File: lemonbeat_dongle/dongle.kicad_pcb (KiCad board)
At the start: 4 copper layers, 50 x 20 mm, 75 parts, among them J201 USB_A, J202 Prog, J203 u.FL, J301 SMA, SW201 SW_Push, U201 nRF52840, U301 Si4467, Y201 32MHz, Y202 32.768kHz, Y301 26MHz

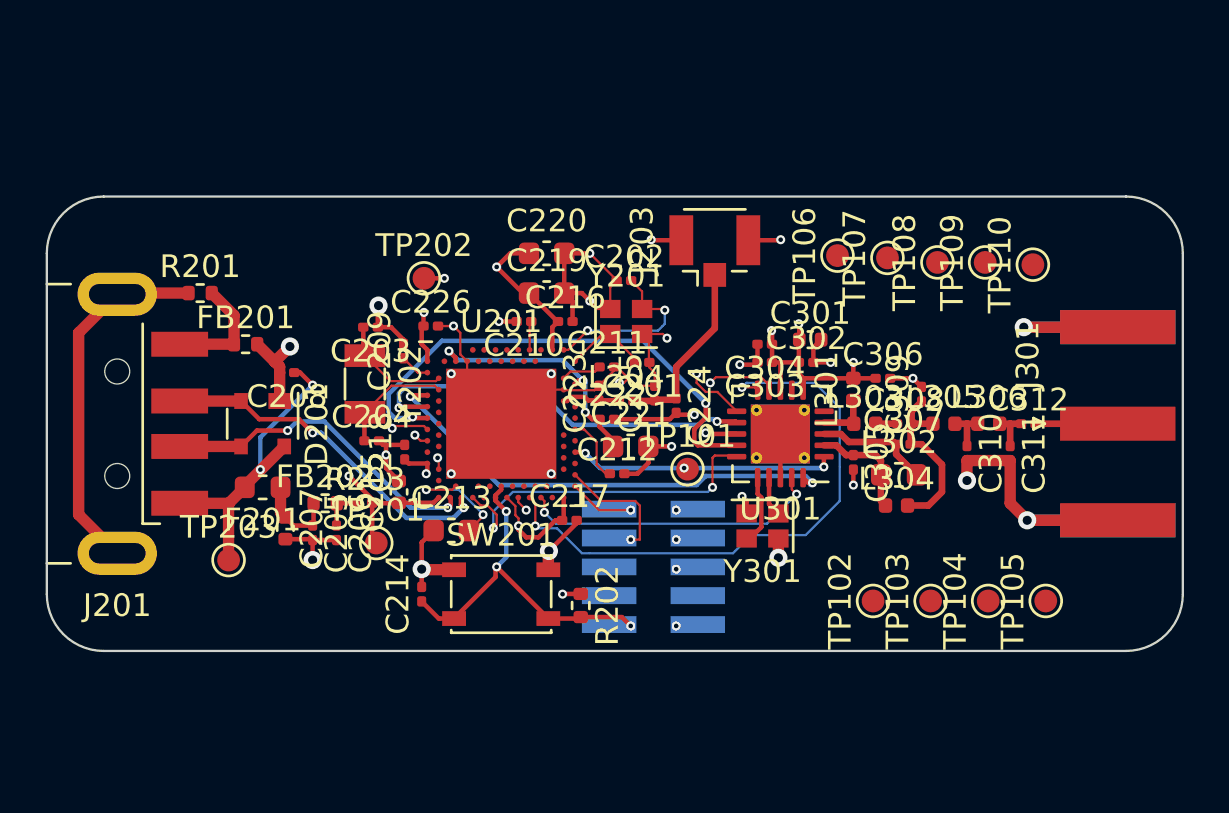
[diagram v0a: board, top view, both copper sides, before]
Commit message: dongle: PCB: add holes in corners
This is in preparation for mounting in a case (e.g. 3D printed).
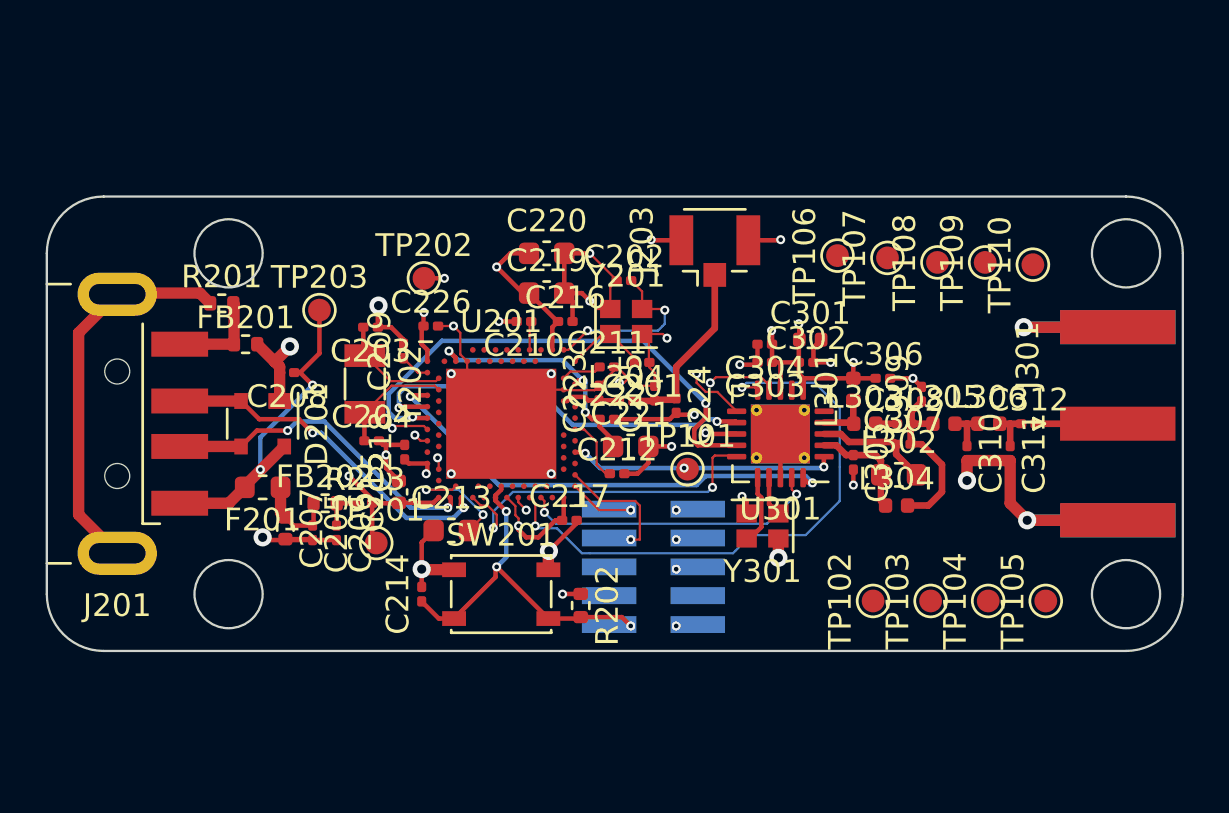
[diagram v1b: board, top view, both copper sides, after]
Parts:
- moved TP203 11.7 mm to (122.5, 99.0)
- moved R201 1.05 mm to (118.2, 98.7)
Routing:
- net GND: track 89.2 -> 90.6 mm
- net Net-(J201-Pad5): track 16.0 -> 17.1 mm
- net Net-(FB201-Pad1): track 5.05 -> 4.20 mm
- net Net-(C208-Pad1): track 13.9 -> 14.5 mm
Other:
- outline, holes or cut-outs redrawn

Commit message: dongle: PCB: add RF guard ring
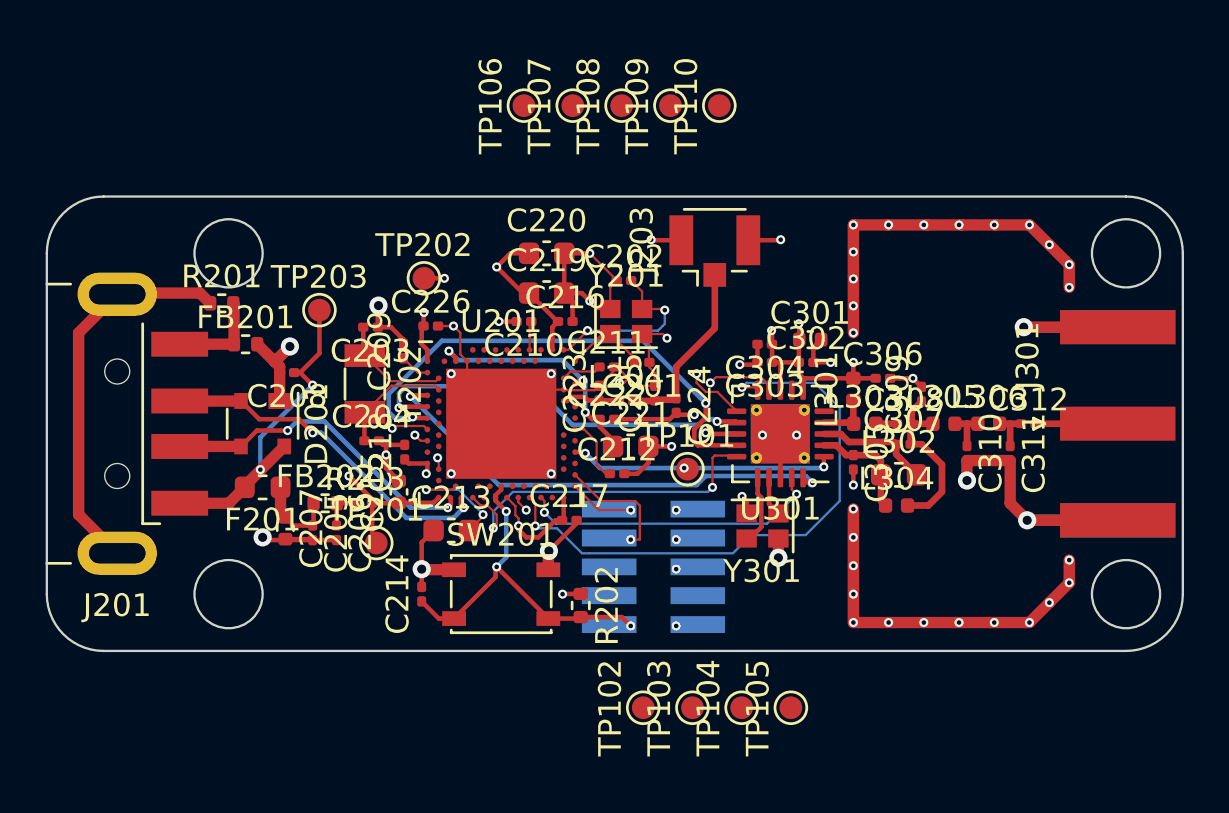
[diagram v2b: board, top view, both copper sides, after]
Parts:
- moved TP108 15.5 mm to (135.8, 90.0)
- moved TP110 15.5 mm to (140.1, 90.0)
- moved TP109 15.5 mm to (137.9, 90.0)
- moved TP107 15.4 mm to (133.7, 90.0)
- moved TP106 15.3 mm to (131.5, 90.0)
- moved TP105 12.2 mm to (143.2, 116.5)
- moved TP104 11.8 mm to (141.1, 116.5)
- moved TP103 11.5 mm to (138.9, 116.5)
- moved TP102 11.2 mm to (136.8, 116.5)
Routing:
- net (no net): track 0.00 -> 32.2 mm, vias 0 -> 26
- net GND: vias 32 -> 34
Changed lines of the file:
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@@
   )
   (footprint "TestPoint:TestPoint_Pad_D1.0mm" (layer "F.Cu")
-    (at 153.9 97 90)
+    (at 140.1 90 90)
     (descr "SMD pad as test Point, diameter 1.0mm")
     (tags "test point SMD pad")
@@
   )
   (footprint "TestPoint:TestPoint_Pad_D1.0mm" (layer "F.Cu")
-    (at 146.866667 111.8 90)
+    (at 136.75 116.5 90)
     (descr "SMD pad as test Point, diameter 1.0mm")
     (tags "test point SMD pad")
@@
   )
   (footprint "TestPoint:TestPoint_Pad_D1.0mm" (layer "F.Cu")
-    (at 154.466667 111.8 90)
+    (at 143.25 116.5 90)
     (descr "SMD pad as test Point, diameter 1.0mm")
     (tags "test point SMD pad")
@@
   )
   (footprint "TestPoint:TestPoint_Pad_D1.0mm" (layer "F.Cu")
-    (at 151.8 96.9 90)
+    (at 137.95 90 90)
     (descr "SMD pad as test Point, diameter 1.0mm")
     (tags "test point SMD pad")
@@
   )
   (footprint "TestPoint:TestPoint_Pad_D1.0mm" (layer "F.Cu")
-    (at 147.5 96.7 90)
+    (at 133.65 90 90)
     (descr "SMD pad as test Point, diameter 1.0mm")
     (tags "test point SMD pad")
@@
   )
   (footprint "TestPoint:TestPoint_Pad_D1.0mm" (layer "F.Cu")
-    (at 149.7 96.9 90)
+    (at 135.8 90 90)
     (descr "SMD pad as test Point, diameter 1.0mm")
     (tags "test point SMD pad")
@@
   )
   (footprint "TestPoint:TestPoint_Pad_D1.0mm" (layer "F.Cu")
-    (at 151.933333 111.8 90)
+    (at 141.083332 116.5 90)
     (descr "SMD pad as test Point, diameter 1.0mm")
     (tags "test point SMD pad")
@@
   )
   (footprint "TestPoint:TestPoint_Pad_D1.0mm" (layer "F.Cu")
-    (at 149.4 111.8 90)
+    (at 138.916666 116.5 90)
     (descr "SMD pad as test Point, diameter 1.0mm")
     (tags "test point SMD pad")
@@
   )
   (footprint "TestPoint:TestPoint_Pad_D1.0mm" (layer "F.Cu")
-    (at 145.3 96.6 90)
+    (at 131.5 90 90)
     (descr "SMD pad as test Point, diameter 1.0mm")
     (tags "test point SMD pad")
@@
     )
   )
+  (gr_line (start 146 95.25) (end 153.75 95.25) (layer "F.Mask") (width 0.5))
+  (gr_line (start 146 107.75) (end 146 112.75) (layer "F.Mask") (width 0.5))
+  (gr_line (start 153.75 95.25) (end 155.5 97) (layer "F.Mask") (width 0.5))
+  (gr_line (start 155.5 97) (end 155.5 98) (layer "F.Mask") (width 0.5))
+  (gr_line (start 146 112.75) (end 153.75 112.75) (layer "F.Mask") (width 0.5))
+  (gr_line (start 153.75 112.75) (end 155.5 111) (layer "F.Mask") (width 0.5))
+  (gr_line (start 155.5 111) (end 155.5 110) (layer "F.Mask") (width 0.5))
+  (gr_line (start 146 100) (end 146 95.25) (layer "F.Mask") (width 0.5))
   (gr_circle (center 158 96.5) (end 159.5 96.5) (layer "Edge.Cuts") (width 0.1) (fill none))
   (gr_arc (start 158 94) (mid 159.767767 94.732233) (end 160.5 96.5) (layer "Edge.Cuts") (width 0.1))
@@
   (gr_arc (start 160.5 111.5) (mid 159.767767 113.267767) (end 158 114) (layer "Edge.Cuts") (width 0.1))
   (gr_line (start 113 94) (end 158 94) (layer "Edge.Cuts") (width 0.1))
+  (segment (start 152.25 95.25) (end 153.75 95.25) (width 0.5) (layer "F.Cu") (net 0))
+  (segment (start 147.5 95.25) (end 149.25 95.25) (width 0.5) (layer "F.Cu") (net 0))
+  (segment (start 154.625 96.125) (end 155.5 97) (width 0.5) (layer "F.Cu") (net 0))
+  (segment (start 146 97.5) (end 146 96.25) (width 0.5) (layer "F.Cu") (net 0))
+  (segment (start 154.625 111.875) (end 153.75 112.75) (width 0.5) (layer "F.Cu") (net 0))
+  (segment (start 147.5 112.75) (end 146 112.75) (width 0.5) (layer "F.Cu") (net 0))
+  (segment (start 146 110.25) (end 146 109) (width 0.5) (layer "F.Cu") (net 0))
+  (segment (start 146 100) (end 146 98.75) (width 0.5) (layer "F.Cu") (net 0))
+  (segment (start 146 98.75) (end 146 97.5) (width 0.5) (layer "F.Cu") (net 0))
+  (segment (start 149.25 95.25) (end 150.75 95.25) (width 0.5) (layer "F.Cu") (net 0))
+  (segment (start 152 112.75) (end 150.5 112.75) (width 0.5) (layer "F.Cu") (net 0))
+  (segment (start 146 112.75) (end 146 111.25) (width 0.5) (layer "F.Cu") (net 0))
+  (segment (start 150.5 112.75) (end 149 112.75) (width 0.5) (layer "F.Cu") (net 0))
+  (segment (start 153.75 112.75) (end 152 112.75) (width 0.5) (layer "F.Cu") (net 0))
+  (segment (start 146 111.25) (end 146 110.25) (width 0.5) (layer "F.Cu") (net 0))
+  (segment (start 146 96.25) (end 146 95.25) (width 0.5) (layer "F.Cu") (net 0))
+  (segment (start 146 109) (end 146 107.75) (width 0.5) (layer "F.Cu") (net 0))
+  (segment (start 149 112.75) (end 147.5 112.75) (width 0.5) (layer "F.Cu") (net 0))
+  (segment (start 155.5 97) (end 155.5 98) (width 0.5) (layer "F.Cu") (net 0))
+  (segment (start 154.625 96.125) (end 153.75 95.25) (width 0.5) (layer "F.Cu") (net 0))
+  (segment (start 155.5 111) (end 155.5 110) (width 0.5) (layer "F.Cu") (net 0))
+  (segment (start 150.75 95.25) (end 152.25 95.25) (width 0.5) (layer "F.Cu") (net 0))
+  (segment (start 155.5 111) (end 154.625 111.875) (width 0.5) (layer "F.Cu") (net 0))
+  (segment (start 146 95.25) (end 147.5 95.25) (width 0.5) (layer "F.Cu") (net 0))
+  (via (at 154.625 96.125) (size 0.4) (drill 0.2) (layers "F.Cu" "B.Cu") (net 0))
+  (via (at 146 98.8125) (size 0.4) (drill 0.2) (layers "F.Cu" "B.Cu") (net 0))
+  (via (at 150.65 95.25) (size 0.4) (drill 0.2) (layers "F.Cu" "B.Cu") (net 0))
+  (via (at 152.2 95.25) (size 0.4) (drill 0.2) (layers "F.Cu" "B.Cu") (net 0))
+  (via (at 146 109) (size 0.4) (drill 0.2) (layers "F.Cu" "B.Cu") (net 0))
+  (via (at 147.55 112.75) (size 0.4) (drill 0.2) (layers "F.Cu" "B.Cu") (net 0))
+  (via (at 146 95.25) (size 0.4) (drill 0.2) (layers "F.Cu" "B.Cu") (net 0))
+  (via (at 152.2 112.75) (size 0.4) (drill 0.2) (layers "F.Cu" "B.Cu") (net 0))
+  (via (at 155.5 111) (size 0.4) (drill 0.2) (layers "F.Cu" "B.Cu") (net 0))
+  (via (at 146 111.5) (size 0.4) (drill 0.2) (layers "F.Cu" "B.Cu") (net 0))
+  (via (at 155.5 97) (size 0.4) (drill 0.2) (layers "F.Cu" "B.Cu") (net 0))
+  (via (at 155.5 110) (size 0.4) (drill 0.2) (layers "F.Cu" "B.Cu") (net 0))
+  (via (at 149.1 95.25) (size 0.4) (drill 0.2) (layers "F.Cu" "B.Cu") (net 0))
+  (via (at 150.65 112.75) (size 0.4) (drill 0.2) (layers "F.Cu" "B.Cu") (net 0))
+  (via (at 146 97.625) (size 0.4) (drill 0.2) (layers "F.Cu" "B.Cu") (net 0))
+  (via (at 146 100) (size 0.4) (drill 0.2) (layers "F.Cu" "B.Cu") (net 0))
+  (via (at 147.55 95.25) (size 0.4) (drill 0.2) (layers "F.Cu" "B.Cu") (net 0))
+  (via (at 153.75 112.75) (size 0.4) (drill 0.2) (layers "F.Cu" "B.Cu") (net 0))
+  (via (at 146 96.4375) (size 0.4) (drill 0.2) (layers "F.Cu" "B.Cu") (net 0))
+  (via (at 146 112.75) (size 0.4) (drill 0.2) (layers "F.Cu" "B.Cu") (net 0))
+  (via (at 149.1 112.75) (size 0.4) (drill 0.2) (layers "F.Cu" "B.Cu") (net 0))
+  (via (at 146 107.75) (size 0.4) (drill 0.2) (layers "F.Cu" "B.Cu") (net 0))
+  (via (at 146 110.25) (size 0.4) (drill 0.2) (layers "F.Cu" "B.Cu") (net 0))
+  (via (at 155.5 98) (size 0.4) (drill 0.2) (layers "F.Cu" "B.Cu") (net 0))
+  (via (at 153.75 95.25) (size 0.4) (drill 0.2) (layers "F.Cu" "B.Cu") (net 0))
+  (via (at 154.625 111.875) (size 0.4) (drill 0.2) (layers "F.Cu" "B.Cu") (net 0))
   (segment (start 122.16 109.08) (end 122.2 109.12) (width 0.2) (layer "F.Cu") (net 1))
   (segment (start 141.3 107.4) (end 141.1 107.2) (width 0.2) (layer "F.Cu") (net 1))
@@
   (via (at 132.7 101.8) (size 0.4) (drill 0.2) (layers "F.Cu" "B.Cu") (net 1))
   (via (at 128.3 101.8) (size 0.4) (drill 0.2) (layers "F.Cu" "B.Cu") (net 1))
+  (via (at 143.5 104.5) (size 0.4) (drill 0.2) (layers "F.Cu" "B.Cu") (net 1))
   (via (at 130.4 99.5) (size 0.4) (drill 0.2) (layers "F.Cu" "B.Cu") (net 1))
   (via (at 132.7 106.2) (size 0.4) (drill 0.2) (layers "F.Cu" "B.Cu") (net 1))
@@
   (via (at 139 103.6) (size 0.4) (drill 0.2) (layers "F.Cu" "B.Cu") (net 1))
   (via (at 153.65 108.25) (size 0.8) (drill 0.4) (layers "F.Cu" "B.Cu") (net 1))
+  (via (at 142 104.5) (size 0.4) (drill 0.2) (layers "F.Cu" "B.Cu") (net 1))
   (via (at 142.8 95.9) (size 0.4) (drill 0.2) (layers "F.Cu" "B.Cu") (net 1))
   (via (at 132.6 109.6) (size 0.8) (drill 0.4) (layers "F.Cu" "B.Cu") (net 1))

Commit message: dongle: PCB: connect RF guard ring to GND net
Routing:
- net (no net): track 32.2 -> 0.00 mm, vias 26 -> 0
- net GND: track 90.6 -> 122.8 mm, vias 34 -> 60

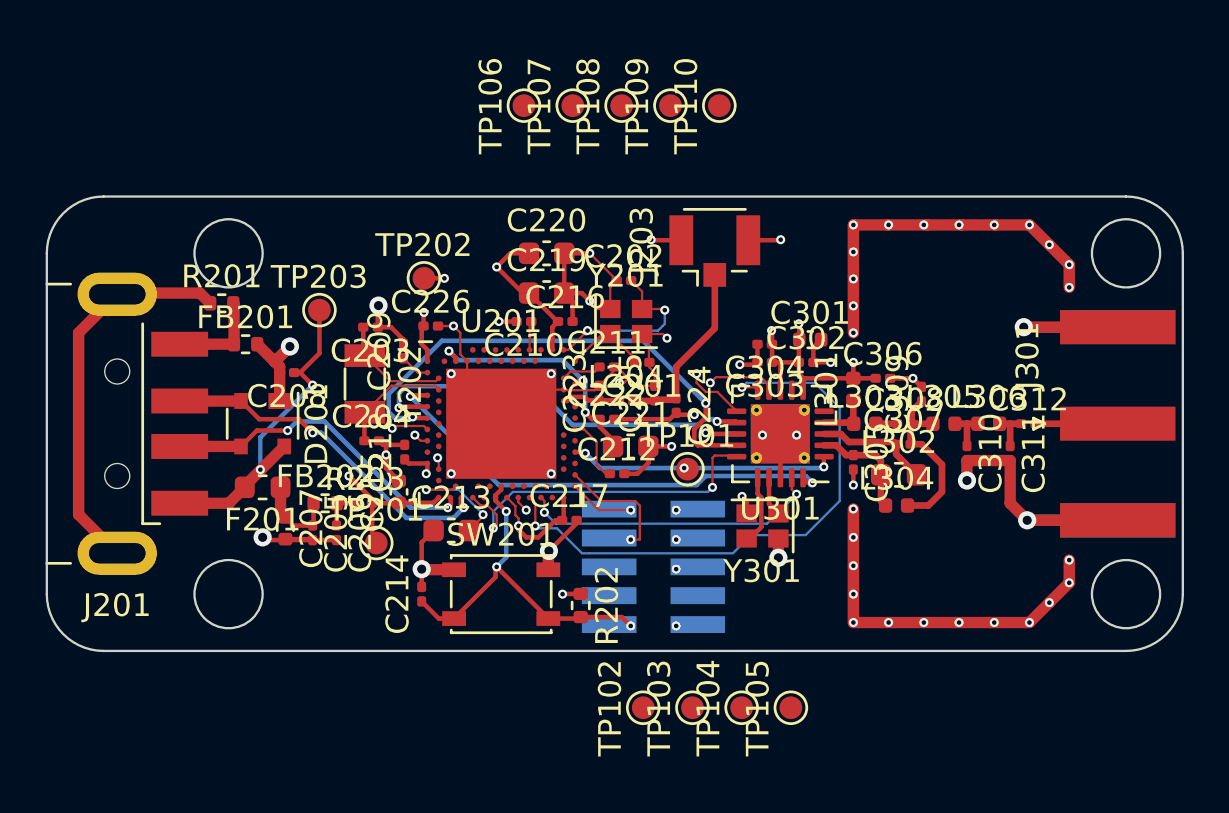
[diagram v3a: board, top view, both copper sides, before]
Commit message: dongle: remove GPIO test points; place other test points on PCB
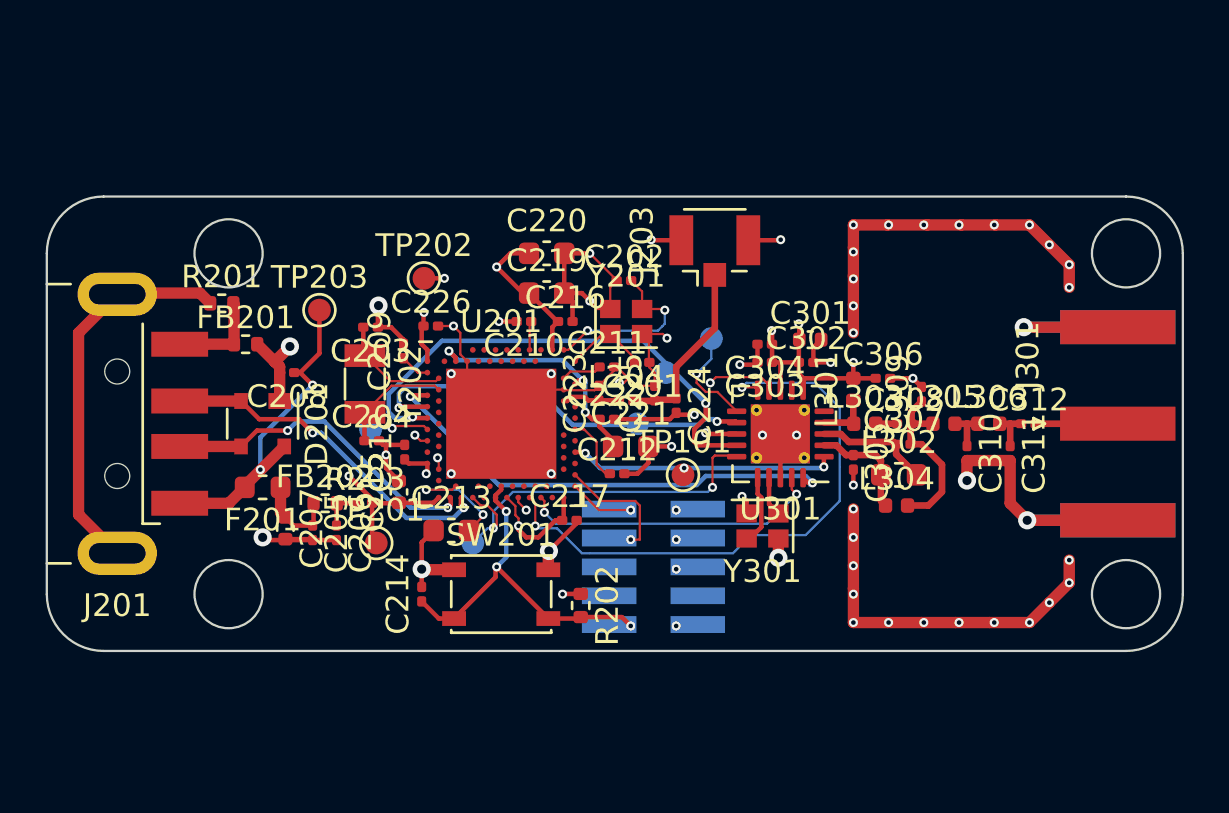
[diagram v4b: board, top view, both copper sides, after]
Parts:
- removed TP107, TP108, TP109, TP110: TestPoint_Small, TestPoint:TestPoint_Pad_D1.0mm
- TP102, TP103, TP104, TP105, TP106: moved to B.Cu
- moved TP104 20.4 mm to (124.8, 104.2), turned to 180 degrees
- moved TP105 15.8 mm to (129.2, 109.2), turned to 180 degrees
- moved TP103 14.8 mm to (137.8, 101.8), turned to 180 degrees
- moved TP106 13.2 mm to (139.8, 100.2), turned to 180 degrees
- moved TP102 12.5 mm to (136.5, 104.0), turned to 180 degrees
- moved TP101 0.32 mm to (138.5, 106.2)
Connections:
- TP102 pad 1: /MCU/P0.20 -> /MCU/P0.04
- TP103 pad 1: /MCU/P0.22 -> /MCU/P0.06
- TP104 pad 1: /MCU/P0.24 -> /MCU/P0.08
- TP105 pad 1: /MCU/P0.26 -> /MCU/P0.13
- TP106 pad 1: /MCU/P0.04 -> /MCU/P1.09
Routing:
- net /MCU/P1.09: track 16.9 -> 18.7 mm
- net /MCU/P0.13: track 15.3 -> 16.4 mm
- net /MCU/P0.08: track 17.4 -> 18.3 mm
